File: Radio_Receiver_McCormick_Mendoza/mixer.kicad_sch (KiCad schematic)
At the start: 0 parts

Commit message: Merge conflict resolution.
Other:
- title: (none) -> Radio Receiver
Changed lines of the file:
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@@
 	(paper "A4")
 	(title_block
+		(title "Radio Receiver")
 		(date "2026-04-19")
 		(rev "0.0.1")

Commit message: Propogated Title Block Fields
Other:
- company: (none) -> Walla Walla University
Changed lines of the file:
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@@
 		(date "2026-04-19")
 		(rev "0.0.1")
+		(company "Walla Walla University")
 		(comment 2 "Daniel Mendoza")
 		(comment 3 "Jeffrey McCormick")

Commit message: Added Tayloe Detector MUX symbol and footprint
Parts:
- added U4: SN74CBT3253CDBR, SN74CBT3253CDBR_1-4_MUX:DB0016A_N, symbol SN74CBT3253CDBR:SN74CBT3253CDBR
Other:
- note added: "Tayloe Detector MUX"
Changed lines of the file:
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@@
 		(comment 3 "Jeffrey McCormick")
 	)
+	(text "Tayloe Detector MUX"
+		(exclude_from_sim no)
+		(at 132.08 55.372 0)
+		(effects
+			(font
+				(size 1.27 1.27)
+			)
+		)
+	)
+	(symbol
+		(lib_id "SN74CBT3253CDBR:SN74CBT3253CDBR")
+		(at 133.35 88.9 0)
+		(unit 1)
+		(body_style 1)
+		(exclude_from_sim no)
+		(in_bom yes)
+		(on_board yes)
+		(in_pos_files yes)
+		(dnp no)
+		(fields_autoplaced yes)
+		(property "Reference" "U4"
+			(at 133.35 60.96 0)
+			(show_name no)
+			(do_not_autoplace no)
+			(effects
+				(font
+					(size 1.524 1.524)
+				)
+			)
+		)
+		(property "Value" "SN74CBT3253CDBR"
+			(at 133.35 63.5 0)
+			(show_name no)
+			(do_not_autoplace no)
+			(effects
+				(font
+					(size 1.524 1.524)
+				)
+			)
+		)
+		(property "Footprint" "SN74CBT3253CDBR_1-4_MUX:DB0016A_N"
+			(at 133.35 88.9 0)
+			(hide yes)
+			(show_name no)
+			(do_not_autoplace no)
+			(effects
+				(font
+					(size 1.27 1.27)
+					(italic yes)
+				)
+			)
+		)
+		(property "Datasheet" "https://www.ti.com/lit/gpn/sn74cbt3253c"
+			(at 133.35 88.9 0)
+			(hide yes)
+			(show_name no)
+			(do_not_autoplace no)
+			(effects
+				(font
+					(size 1.27 1.27)
+					(italic yes)
+				)
+			)
+		)
+		(property "Description" "Multiplexer/Demultiplexer 2 x 4:1 16-SSOP"
+			(at 133.35 88.9 0)
+			(hide yes)
+			(show_name no)
+			(do_not_autoplace no)
+			(effects
+				(font
+					(size 1.27 1.27)
+				)
+			)
+		)
+		(pin "11"
+		)
+		(pin "1"
+		)
+		(pin "13"
+		)
+		(pin "7"
+		)
+		(pin "14"
+		)
+		(pin "12"
+		)
+		(pin "2"
+		)
+		(pin "4"
+		)
+		(pin "3"
+		)
+		(pin "9"
+		)
+		(pin "10"
+		)
+		(pin "8"
+		)
+		(pin "15"
+		)
+		(pin "16"
+		)
+		(pin "6"
+		)
+		(pin "5"
+		)
+		(instances
+			(project "Radio_Receiver_McCormick_Mendoza"
+				(path "/f31d31ab-6846-4f3a-92b1-aa5a6a13373f/132a78a3-63a8-4709-a5ba-2b34eb7966d9"
+					(reference "U4")
+					(unit 1)
+				)
+			)
+		)
+	)
 )

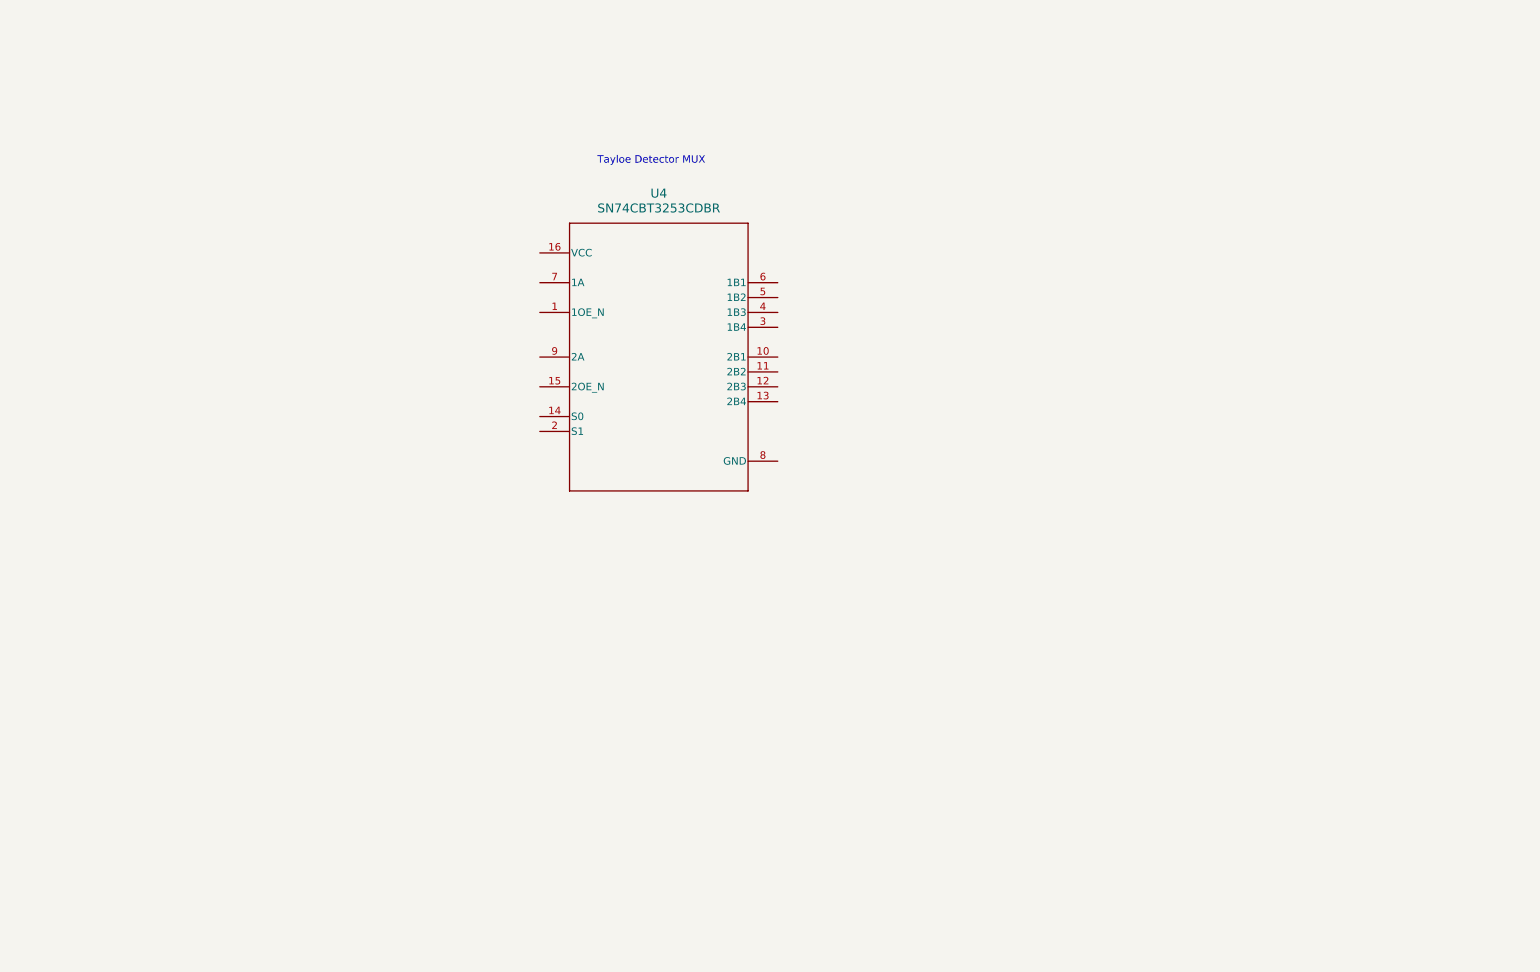
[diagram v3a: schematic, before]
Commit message: Added Daniel Mendoza's changes to KiCAD files.
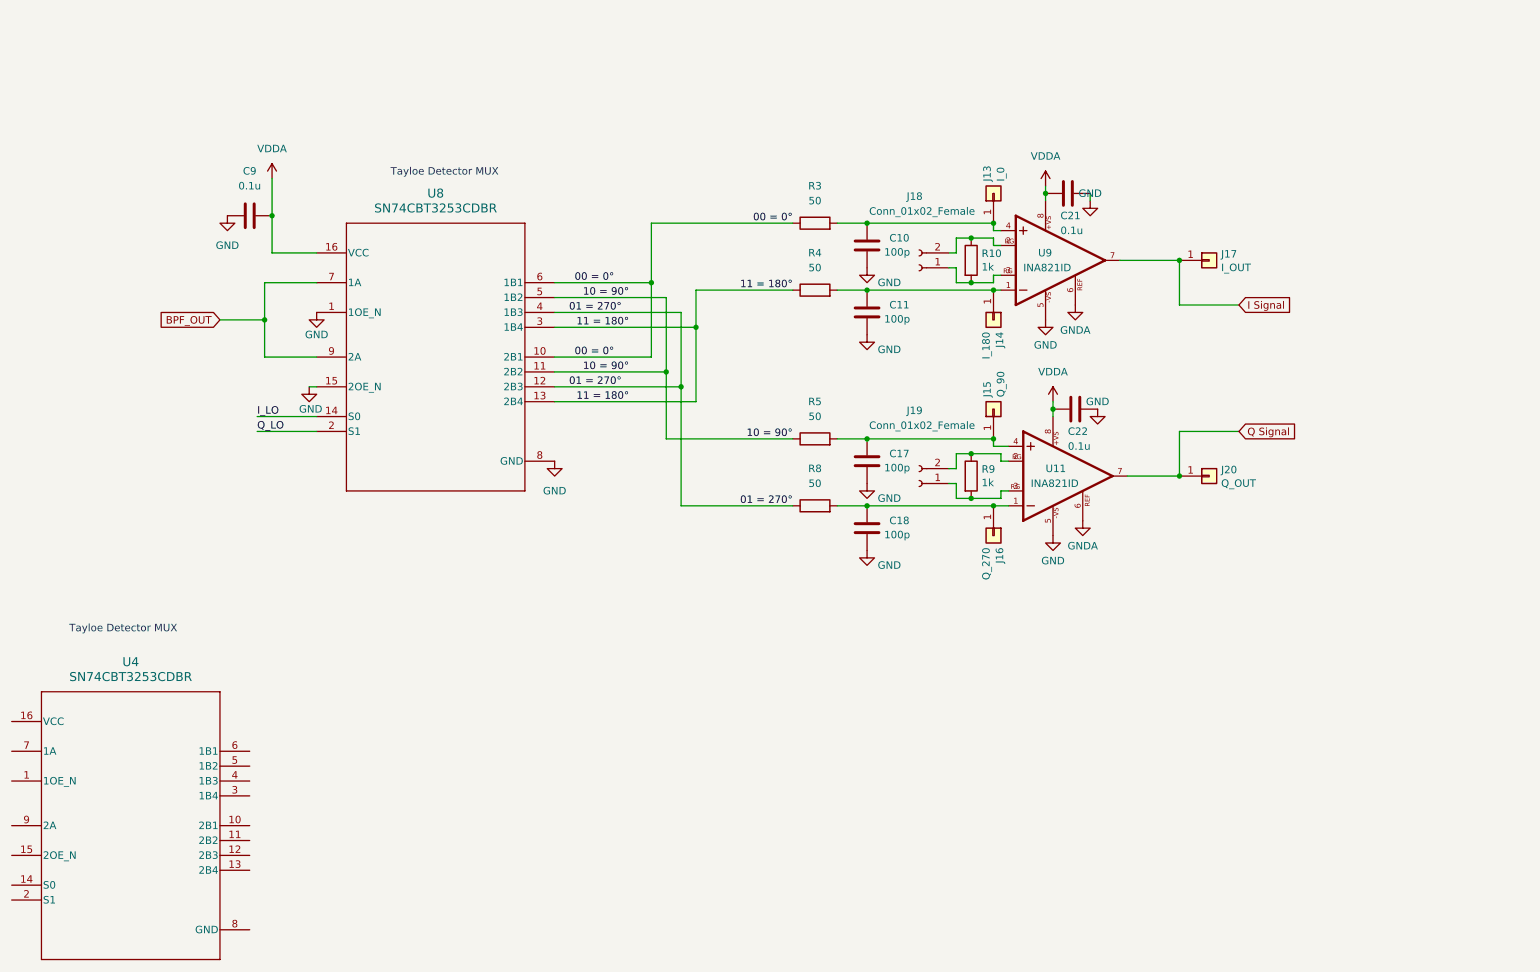
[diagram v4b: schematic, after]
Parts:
- added C10, C11, C17, C18: 100p, Capacitor_THT:C_Disc_D5.0mm_W2.5mm_P2.50mm, symbol Device:C
- added C21, C22, C9: 0.1u, Capacitor_THT:C_Disc_D5.1mm_W3.2mm_P5.00mm, symbol Device:C
- added J13: I_0, Connector_PinHeader_2.54mm:PinHeader_1x01_P2.54mm_Vertical, symbol Connector_Generic:Conn_01x01
- added J14: I_180, Connector_PinHeader_2.54mm:PinHeader_1x01_P2.54mm_Vertical, symbol Connector_Generic:Conn_01x01
- added J15: Q_90, Connector_PinHeader_2.54mm:PinHeader_1x01_P2.54mm_Vertical, symbol Connector_Generic:Conn_01x01
- added J16: Q_270, Connector_PinHeader_2.54mm:PinHeader_1x01_P2.54mm_Vertical, symbol Connector_Generic:Conn_01x01
- added J17: I_OUT, Connector_PinHeader_2.54mm:PinHeader_1x01_P2.54mm_Vertical, symbol Connector_Generic:Conn_01x01
- added J18, J19: Conn_01x02_Female, Connector_PinSocket_2.54mm:PinSocket_1x02_P2.54mm_Vertical, symbol Connector:Conn_01x02_Female
- added J20: Q_OUT, Connector_PinHeader_2.54mm:PinHeader_1x01_P2.54mm_Vertical, symbol Connector_Generic:Conn_01x01
- added R10, R9: 1k, Resistor_THT:R_Axial_DIN0207_L6.3mm_D2.5mm_P7.62mm_Horizontal, symbol Device:R
- added R3, R4, R5, R8: 50, symbol Device:R
- added U11, U9: INA821ID, import_footprint:SOIC127P600X175-8N, symbol INA821ID:INA821ID
- added U8: SN74CBT3253CDBR, SN74CBT3253CDBR_1-4_MUX:DB0016A_N, symbol SN74CBT3253CDBR:SN74CBT3253CDBR
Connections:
- new net: J19.1 (Pin_1), R9.2, U11.3 (RG1)
- new net: J19.2 (Pin_2), R9.1, U11.2 (RG)
- new net: C18.1, J16.1 (Pin_1), R8.2, U11.1 (-IN)
- new net: C17.1, J15.1 (Pin_1), R5.2, U11.4 (+IN)
- new net: C10.1, J13.1 (Pin_1), R3.2, U9.4 (+IN)
- new net: J18.2 (Pin_2), R10.1, U9.2 (RG)
- new net: J18.1 (Pin_1), R10.2, U9.3 (RG1)
- new net: C11.1, J14.1 (Pin_1), R4.2, U9.1 (-IN)
- new net 00 = 0°: R3.1, U8.10 (2B1), U8.6 (1B1)
- new net 01 = 270°: R8.1, U8.12 (2B3), U8.4 (1B3)
- new net 10 = 90°: R5.1, U8.11 (2B2), U8.5 (1B2)
- new net 11 = 180°: R4.1, U8.13 (2B4), U8.3 (1B4)
- new net BPF_OUT: U8.7 (1A), U8.9 (2A)
- new net GND: C10.2, C11.2, C17.2, C18.2, C21.1, C22.1, C9.1, U11.5 (-VS), U8.1 (1OE_N), U8.15 (2OE_N), U8.8 (GND), U9.5 (-VS)
- new net GNDA: U11.6 (REF), U9.6 (REF)
- new net I Signal: J17.1 (Pin_1), U9.7 (OUT)
- new net I_LO: U8.14 (S0)
- new net Q Signal: J20.1 (Pin_1), U11.7 (OUT)
- new net Q_LO: U8.2 (S1)
- new net VDDA: C21.2, C22.2, C9.2, U11.8 (+VS), U8.16 (VCC), U9.8 (+VS)
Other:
- moved on the sheet: U4

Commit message: Added switchable antenna filters and photos.
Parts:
- removed U4: SN74CBT3253CDBR, SN74CBT3253CDBR_1-4_MUX:DB0016A_N, symbol SN74CBT3253CDBR:SN74CBT3253CDBR
- R10, R9: value 1k -> 33
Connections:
- net GNDA is gone; now on net GND: U11.6 (REF), U9.6 (REF)
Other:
- note added: "GNDA?"
- note added: "Justified? Confirm gain in LTSpice"
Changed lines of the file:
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@@
 	(text "Tayloe Detector MUX"
 		(exclude_from_sim no)
-		(at 41.91 135.382 0)
+		(at 96.774 57.404 0)
 		(effects
 			(font
@@
 		)
 	)
-	(text "Tayloe Detector MUX"
+	(text "GNDA?"
 		(exclude_from_sim no)
-		(at 96.774 57.404 0)
+		(at 208.28 80.518 0)
+		(effects
+			(font
+				(size 1.27 1.27)
+			)
+		)
+	)
+	(text "GNDA?"
+		(exclude_from_sim no)
+		(at 209.296 117.348 0)
+		(effects
+			(font
+				(size 1.27 1.27)
+			)
+		)
+	)
+	(text "Justified?\nConfirm gain\nin LTSpice"
+		(exclude_from_sim no)
+		(at 174.244 50.546 0)
 		(effects
 			(font
@@
 		)
 	)
+	(polyline
+		(pts
+			(xy 179.07 54.61) (xy 179.07 105.41)
+		)
+		(stroke
+			(width 0)
+			(type dash)
+		)
+	)
 	(wire
 		(pts
@@
 		)
 	)
+	(polyline
+		(pts
+			(xy 186.69 54.61) (xy 186.69 67.31)
+		)
+		(stroke
+			(width 0)
+			(type dash)
+		)
+	)
 	(wire
 		(pts
@@
 		)
 	)
+	(polyline
+		(pts
+			(xy 178.435 54.61) (xy 186.69 54.61)
+		)
+		(stroke
+			(width 0)
+			(type dash)
+		)
+	)
 	(wire
 		(pts
@@
 		)
 	)
+	(polyline
+		(pts
+			(xy 179.07 105.41) (xy 182.88 105.41)
+		)
+		(stroke
+			(width 0)
+			(type default)
+		)
+	)
 	(wire
 		(pts
@@
 		)
 		(property "Value" "GND"
-			(at 207.01 60.96 0)
+			(at 207.264 59.69 0)
 			(show_name no)
 			(do_not_autoplace no)
@@
 			)
 		)
-		(property "Value" "1k"
+		(property "Value" "33"
 			(at 188.468 73.533 0)
 			(show_name no)
@@
 			)
 		)
-		(property "Value" "1k"
+		(property "Value" "33"
 			(at 188.468 110.363 0)
 			(show_name no)
@@
 	)
 	(symbol
-		(lib_id "SN74CBT3253CDBR:SN74CBT3253CDBR")
-		(at 43.18 168.91 0)
-		(unit 1)
-		(body_style 1)
-		(exclude_from_sim no)
-		(in_bom yes)
-		(on_board yes)
-		(in_pos_files yes)
-		(dnp no)
-		(fields_autoplaced yes)
-		(property "Reference" "U4"
-			(at 43.18 140.97 0)
-			(show_name no)
-			(do_not_autoplace no)
-			(effects
-				(font
-					(size 1.524 1.524)
-				)
-			)
-		)
-		(property "Value" "SN74CBT3253CDBR"
-			(at 43.18 143.51 0)
-			(show_name no)
-			(do_not_autoplace no)
-			(effects
-				(font
-					(size 1.524 1.524)
-				)
-			)
-		)
-		(property "Footprint" "SN74CBT3253CDBR_1-4_MUX:DB0016A_N"
-			(at 43.18 168.91 0)
-			(hide yes)
-			(show_name no)
-			(do_not_autoplace no)
-			(effects
-				(font
-					(size 1.27 1.27)
-					(italic yes)
-				)
-			)
-		)
-		(property "Datasheet" "https://www.ti.com/lit/gpn/sn74cbt3253c"
-			(at 43.18 168.91 0)
-			(hide yes)
-			(show_name no)
-			(do_not_autoplace no)
-			(effects
-				(font
-					(size 1.27 1.27)
-					(italic yes)
-				)
-			)
-		)
-		(property "Description" "Multiplexer/Demultiplexer 2 x 4:1 16-SSOP"
-			(at 43.18 168.91 0)
-			(hide yes)
-			(show_name no)
-			(do_not_autoplace no)
-			(effects
-				(font
-					(size 1.27 1.27)
-				)
-			)
-		)
-		(pin "11"
-		)
-		(pin "1"
-		)
-		(pin "13"
-		)
-		(pin "7"
-		)
-		(pin "14"
-		)
-		(pin "12"
-		)
-		(pin "2"
-		)
-		(pin "4"
-		)
-		(pin "3"
-		)
-		(pin "9"
-		)
-		(pin "10"
-		)
-		(pin "8"
-		)
-		(pin "15"
-		)
-		(pin "16"
-		)
-		(pin "6"
-		)
-		(pin "5"
-		)
-		(instances
-			(project "Radio_Receiver_McCormick_Mendoza"
-				(path "/f31d31ab-6846-4f3a-92b1-aa5a6a13373f/132a78a3-63a8-4709-a5ba-2b34eb7966d9"
-					(reference "U4")
-					(unit 1)
-				)
-			)
-		)
-	)
-	(symbol
 		(lib_id "Device:R")
 		(at 160.02 102.87 90)
@@
 			)
 		)
-		(property "Value" "GNDA"
+		(property "Value" "GND"
 			(at 205.74 121.158 0)
 			(show_name no)
@@
 			)
 		)
-		(property "Value" "GNDA"
+		(property "Value" "GND"
 			(at 204.47 84.328 0)
 			(show_name no)

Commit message: Schematic connection edits
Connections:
- net I Signal renamed I_Signal
- net Q Signal renamed Q_Signal
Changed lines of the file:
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@@
-		)
-	)
-	(label "I_LO"
-		(at 64.77 99.06 0)
-		(effects
-			(font
-				(size 1.27 1.27)
-			)
-			(justify left bottom)
-		)
-	)
-	(label "Q_LO"
-		(at 64.77 101.6 0)
-		(effects
-			(font
-				(size 1.27 1.27)
-			)
-			(justify left bottom)
 		)
 	)
@@
 		)
 	)
-	(global_label "I Signal"
-		(shape input)
+	(global_label "I_Signal"
+		(shape output)
 		(at 232.41 80.01 0)
 		(fields_autoplaced yes)
@@
 		)
 	)
-	(global_label "Q Signal"
-		(shape input)
+	(global_label "Q_Signal"
+		(shape output)
 		(at 232.41 101.6 0)
 		(fields_autoplaced yes)
@@
 			(hide yes)
 			(show_name no)
+			(do_not_autoplace no)
+			(effects
+				(font
+					(size 1.27 1.27)
+				)
+				(justify right)
+			)
+		)
+	)
+	(global_label "I_LO"
+		(shape input)
+		(at 64.77 99.06 180)
+		(fields_autoplaced yes)
+		(effects
+			(font
+				(size 1.27 1.27)
+			)
+			(justify right)
+		)
+		(property "Intersheetrefs" "${INTERSHEET_REFS}"
+			(at 57.8538 99.06 0)
+			(hide yes)
+			(show_name no)
+			(do_not_autoplace no)
+			(effects
+				(font
+					(size 1.27 1.27)
+				)
+				(justify right)
+			)
+		)
+	)
+	(global_label "Q_LO"
+		(shape input)
+		(at 64.77 101.6 180)
+		(fields_autoplaced yes)
+		(effects
+			(font
+				(size 1.27 1.27)
+			)
+			(justify right)
+		)
+		(property "Intersheetrefs" "${INTERSHEET_REFS}"
+			(at 57.1281 101.6 0)
+			(hide yes)
+			(show_name no)

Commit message: Schematic edits power and signal systems
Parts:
- removed R3, R4, R5, R8: 50, symbol Device:R
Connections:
- net 00 = 0°: now also C10.1, J13.1 (Pin_1), U9.4 (+IN)
- net 01 = 270°: now also C18.1, J16.1 (Pin_1), U11.1 (-IN)
- net 10 = 90°: now also C17.1, J15.1 (Pin_1), U11.4 (+IN)
- net 11 = 180°: now also C11.1, J14.1 (Pin_1), U9.1 (-IN)
- net BPF_OUT renamed BPF_OUT1
- net BPF_OUT1: no longer U8.9 (2A)
- net I_Signal renamed I_OUT
- net Q_Signal renamed Q_OUT
- new net BPF_OUT2: U8.9 (2A)
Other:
- note added: "Gain: G = 1+49.4kΩ/Rg"
- note removed: "GNDA?"
